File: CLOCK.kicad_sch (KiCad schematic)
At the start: 36 parts, among them U15 PL133-37, U5 TLV70033DDCR, X1 SIT2001BC-S2-33N-21.477270

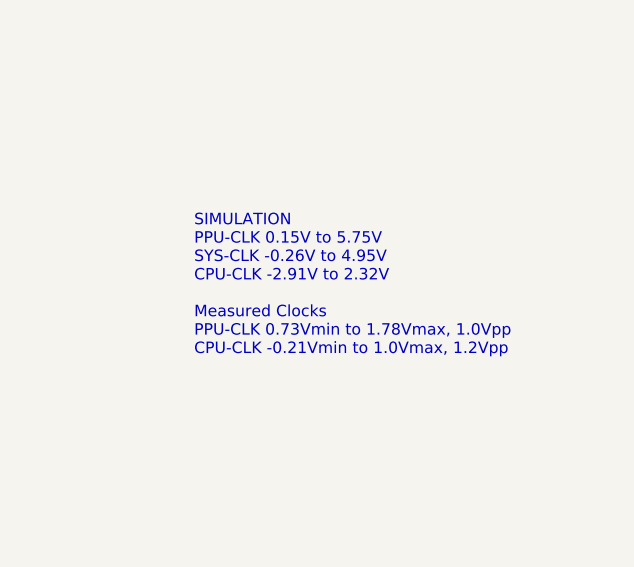
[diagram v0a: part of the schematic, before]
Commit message: rev2 sent to fab
Added CHR RAM.
Changed board to 4 layers (was 2 layers).
Changed passives to 0603 (was 0402)
Fixed CIRAM-A10 not being hooked up
Fixed PPU-A10..A12 being hooked to VRAM but should have been.
Added more silkscreen for easier debugging.
Added filter inductor to 5V from USB-C.
Changed video out to stock (was THS7374)
Changed audio circuit to stock (was headphone amp IC)
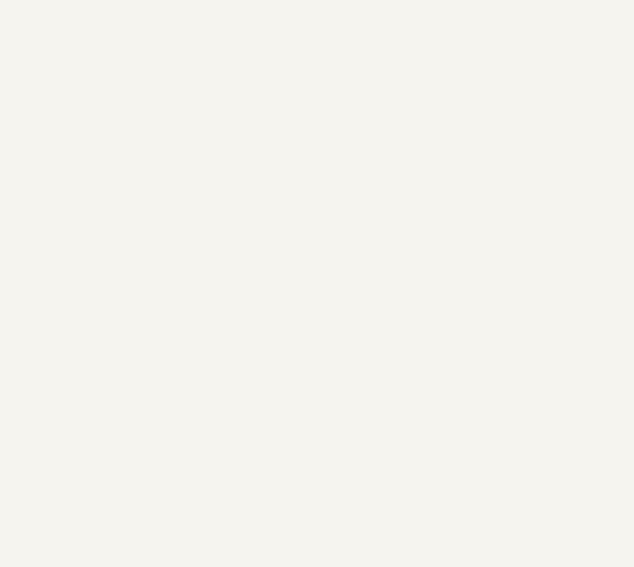
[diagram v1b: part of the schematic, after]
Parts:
- C14, C33: footprint Capacitor_SMD:C_0402_1005Metric -> Capacitor_SMD:C_0603_1608Metric_Pad1.08x0.95mm_HandSolder; Digikey 490-3890-2-ND -> (none); MPN GRM155R61A105KE15D -> (none); Size 0402 -> (none)
- C19, C28, C34, C6, C9: footprint Capacitor_SMD:C_0402_1005Metric -> Capacitor_SMD:C_0603_1608Metric_Pad1.08x0.95mm_HandSolder; Digikey 1276-1509-2-ND -> (none); MPN CL05B104KO5NNWC -> (none); QOH 10000 -> (none)
- R21: footprint Resistor_SMD:R_0402_1005Metric -> Resistor_SMD:R_0603_1608Metric_Pad0.98x0.95mm_HandSolder; Digikey P10.0KLCT-ND -> (none); MPN ERJ-2RKF1002X -> (none)
- R22, R29: footprint Resistor_SMD:R_0402_1005Metric -> Resistor_SMD:R_0603_1608Metric_Pad0.98x0.95mm_HandSolder; Digikey 311-30JRCT-ND -> (none); MPN RC0402JR-0730RL -> (none)
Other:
- note removed: "SIMULATION PPU-CLK 0.15V to 5.75V SYS-CLK -0.26V to 4.95V CPU-CLK -2.91V to 2.32V Measured Clocks PPU-CLK 0.73Vmin to 1.78Vmax, 1.0Vpp CPU-CLK -0.21Vmin to 1.0Vmax, 1.2Vpp"

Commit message: filled out BOM
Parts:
- C14, C33: Digikey (none) -> 1276-1102-1-ND; MPN (none) -> CL10A105KA8NNNC
- C19, C28, C34, C6, C9: Digikey (none) -> 1276-CL10B104KB8WPNDCT-ND; MPN (none) -> CL10B104KB8WPND
- R21: Digikey (none) -> RMCF0603FT10K0CT-ND; MPN (none) -> RMCF0603FT10K0
- R22, R29: Digikey (none) -> 738-RMCF0603FT30R0CT-ND; MPN (none) -> RMCF0603FT30R0
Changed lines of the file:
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@@
   (title_block
     (title "InGame-NES MMC3")
-    (date "2022-06-03")
-    (rev "1")
+    (date "2022-08-02")
+    (rev "2")
     (company "Late to the Game")
   )
@@
       (effects (font (size 1.27 1.27)) hide)
     )
-    (property "Description" "CAP CER 1UF 25V X7R 0603" (id 4) (at 181.61 83.82 0)
+    (property "Description" "CAP CER 1UF 25V X5R 0603" (id 4) (at 181.61 83.82 0)
       (effects (font (size 1.27 1.27)) hide)
     )
@@
       (effects (font (size 1.27 1.27)) hide)
     )
-    (property "Digikey" "" (id 6) (at 181.61 83.82 0)
-      (effects (font (size 1.27 1.27)) hide)
-    )
-    (property "MPN" "" (id 7) (at 181.61 83.82 0)
+    (property "Digikey" "1276-1102-1-ND" (id 6) (at 181.61 83.82 0)
+      (effects (font (size 1.27 1.27)) hide)
+    )
+    (property "MPN" "CL10A105KA8NNNC" (id 7) (at 181.61 83.82 0)
       (effects (font (size 1.27 1.27)) hide)
     )
@@
       (effects (font (size 1.27 1.27)) hide)
     )
-    (property "Description" "CAP CER 0.1UF 16V X7R 0402" (id 4) (at 120.65 123.19 0)
+    (property "Description" "CAP CER 0.1UF 50V X7R 0603" (id 4) (at 120.65 123.19 0)
       (effects (font (size 1.27 1.27)) hide)
     )
@@
       (effects (font (size 1.27 1.27)) hide)
     )
-    (property "Digikey" "" (id 6) (at 120.65 123.19 0)
-      (effects (font (size 1.27 1.27)) hide)
-    )
-    (property "MPN" "" (id 7) (at 120.65 123.19 0)
+    (property "Digikey" "1276-CL10B104KB8WPNDCT-ND" (id 6) (at 120.65 123.19 0)
+      (effects (font (size 1.27 1.27)) hide)
+    )
+    (property "MPN" "CL10B104KB8WPND" (id 7) (at 120.65 123.19 0)
       (effects (font (size 1.27 1.27)) hide)
     )
@@
       (effects (font (size 1.27 1.27)) hide)
     )
-    (property "Description" "RES 30 OHM" (id 4) (at 189.23 142.24 0)
-      (effects (font (size 1.27 1.27)) hide)
-    )
-    (property "Digikey" "" (id 5) (at 189.23 142.24 0)
-      (effects (font (size 1.27 1.27)) hide)
-    )
-    (property "MPN" "" (id 6) (at 189.23 142.24 0)
+    (property "Description" "RES SMD 30 OHM 1% 1/10W 0603" (id 4) (at 189.23 142.24 0)
+      (effects (font (size 1.27 1.27)) hide)
+    )
+    (property "Digikey" "738-RMCF0603FT30R0CT-ND" (id 5) (at 189.23 142.24 0)
+      (effects (font (size 1.27 1.27)) hide)
+    )
+    (property "MPN" "RMCF0603FT30R0" (id 6) (at 189.23 142.24 0)
       (effects (font (size 1.27 1.27)) hide)
     )
@@
       (effects (font (size 1.27 1.27)) hide)
     )
-    (property "Description" "CAP CER 0.1UF 16V X7R 0402" (id 4) (at 158.75 83.82 0)
+    (property "Description" "CAP CER 0.1UF 50V X7R 0603" (id 4) (at 158.75 83.82 0)
       (effects (font (size 1.27 1.27)) hide)
     )
@@
       (effects (font (size 1.27 1.27)) hide)
     )
-    (property "Digikey" "" (id 6) (at 158.75 83.82 0)
-      (effects (font (size 1.27 1.27)) hide)
-    )
-    (property "MPN" "" (id 7) (at 158.75 83.82 0)
+    (property "Digikey" "1276-CL10B104KB8WPNDCT-ND" (id 6) (at 158.75 83.82 0)
+      (effects (font (size 1.27 1.27)) hide)
+    )
+    (property "MPN" "CL10B104KB8WPND" (id 7) (at 158.75 83.82 0)
       (effects (font (size 1.27 1.27)) hide)
     )
@@
       (effects (font (size 1.27 1.27)) hide)
     )
-    (property "Description" "RES 30 OHM" (id 4) (at 189.23 139.7 0)
-      (effects (font (size 1.27 1.27)) hide)
-    )
-    (property "Digikey" "" (id 5) (at 189.23 139.7 0)
-      (effects (font (size 1.27 1.27)) hide)
-    )
-    (property "MPN" "" (id 6) (at 189.23 139.7 0)
+    (property "Description" "RES SMD 30 OHM 1% 1/10W 0603" (id 4) (at 189.23 139.7 0)
+      (effects (font (size 1.27 1.27)) hide)
+    )
+    (property "Digikey" "738-RMCF0603FT30R0CT-ND" (id 5) (at 189.23 139.7 0)
+      (effects (font (size 1.27 1.27)) hide)
+    )
+    (property "MPN" "RMCF0603FT30R0" (id 6) (at 189.23 139.7 0)
       (effects (font (size 1.27 1.27)) hide)
     )
@@
       (effects (font (size 1.27 1.27)) hide)
     )
-    (property "Description" "RES 10K OHM" (id 4) (at 109.22 129.54 0)
-      (effects (font (size 1.27 1.27)) hide)
-    )
-    (property "Digikey" "" (id 5) (at 109.22 129.54 0)
-      (effects (font (size 1.27 1.27)) hide)
-    )
-    (property "MPN" "" (id 6) (at 109.22 129.54 0)
+    (property "Description" "RES SMD 10K OHM 1% 1/10W 0603" (id 4) (at 109.22 129.54 0)
+      (effects (font (size 1.27 1.27)) hide)
+    )
+    (property "Digikey" "RMCF0603FT10K0CT-ND" (id 5) (at 109.22 129.54 0)
+      (effects (font (size 1.27 1.27)) hide)
+    )
+    (property "MPN" "RMCF0603FT10K0" (id 6) (at 109.22 129.54 0)
       (effects (font (size 1.27 1.27)) hide)
     )
@@
       (effects (font (size 1.27 1.27)) hide)
     )
-    (property "Description" "CAP CER 0.1UF 16V X7R 0402" (id 4) (at 115.57 83.82 0)
+    (property "Description" "CAP CER 0.1UF 50V X7R 0603" (id 4) (at 115.57 83.82 0)
       (effects (font (size 1.27 1.27)) hide)
     )
@@
       (effects (font (size 1.27 1.27)) hide)
     )
-    (property "Digikey" "" (id 6) (at 115.57 83.82 0)
-      (effects (font (size 1.27 1.27)) hide)
-    )
-    (property "MPN" "" (id 7) (at 115.57 83.82 0)
+    (property "Digikey" "1276-CL10B104KB8WPNDCT-ND" (id 6) (at 115.57 83.82 0)
+      (effects (font (size 1.27 1.27)) hide)
+    )
+    (property "MPN" "CL10B104KB8WPND" (id 7) (at 115.57 83.82 0)
       (effects (font (size 1.27 1.27)) hide)
     )
@@
       (effects (font (size 1.27 1.27)) hide)
     )
-    (property "Description" "CAP CER 0.1UF 16V X7R 0402" (id 4) (at 181.61 120.65 0)
+    (property "Description" "CAP CER 0.1UF 50V X7R 0603" (id 4) (at 181.61 120.65 0)
       (effects (font (size 1.27 1.27)) hide)
     )
@@
       (effects (font (size 1.27 1.27)) hide)
     )
-    (property "Digikey" "" (id 6) (at 181.61 120.65 0)
-      (effects (font (size 1.27 1.27)) hide)
-    )
-    (property "MPN" "" (id 7) (at 181.61 120.65 0)
+    (property "Digikey" "1276-CL10B104KB8WPNDCT-ND" (id 6) (at 181.61 120.65 0)
+      (effects (font (size 1.27 1.27)) hide)
+    )
+    (property "MPN" "CL10B104KB8WPND" (id 7) (at 181.61 120.65 0)
       (effects (font (size 1.27 1.27)) hide)
     )
@@
       (effects (font (size 1.27 1.27)) hide)
     )
-    (property "Description" "CAP CER 0.1UF 16V X7R 0402" (id 4) (at 170.18 83.82 0)
+    (property "Description" "CAP CER 0.1UF 50V X7R 0603" (id 4) (at 170.18 83.82 0)
       (effects (font (size 1.27 1.27)) hide)
     )
@@
       (effects (font (size 1.27 1.27)) hide)
     )
-    (property "Digikey" "" (id 6) (at 170.18 83.82 0)
-      (effects (font (size 1.27 1.27)) hide)
-    )
-    (property "MPN" "" (id 7) (at 170.18 83.82 0)
+    (property "Digikey" "1276-CL10B104KB8WPNDCT-ND" (id 6) (at 170.18 83.82 0)
+      (effects (font (size 1.27 1.27)) hide)
+    )
+    (property "MPN" "CL10B104KB8WPND" (id 7) (at 170.18 83.82 0)
       (effects (font (size 1.27 1.27)) hide)
     )
@@
       (effects (font (size 1.27 1.27)) hide)
     )
-    (property "Description" "CAP CER 1UF 25V X7R 0603" (id 4) (at 127 83.82 0)
+    (property "Description" "CAP CER 1UF 25V X5R 0603" (id 4) (at 127 83.82 0)
       (effects (font (size 1.27 1.27)) hide)
     )
@@
       (effects (font (size 1.27 1.27)) hide)
     )
-    (property "Digikey" "" (id 6) (at 127 83.82 0)
-      (effects (font (size 1.27 1.27)) hide)
-    )
-    (property "MPN" "" (id 7) (at 127 83.82 0)
-      (effects (font (size 1.27 1.27)) hide)
-    )
+    (property "Digikey" "1276-1102-1-ND" (id 6) (at 127 83.82 0)
+      (effects (font (size 1.27 1.27)) hide)
+    )
+    (property "MPN" "CL10A105KA8NNNC" (id 7) (at 127 83.82 0)
+      (effects (font (size 1.27 1.27)) hide)
+    )
